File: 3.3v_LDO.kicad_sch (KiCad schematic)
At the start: 7 parts, among them U2 LP2985-3.3

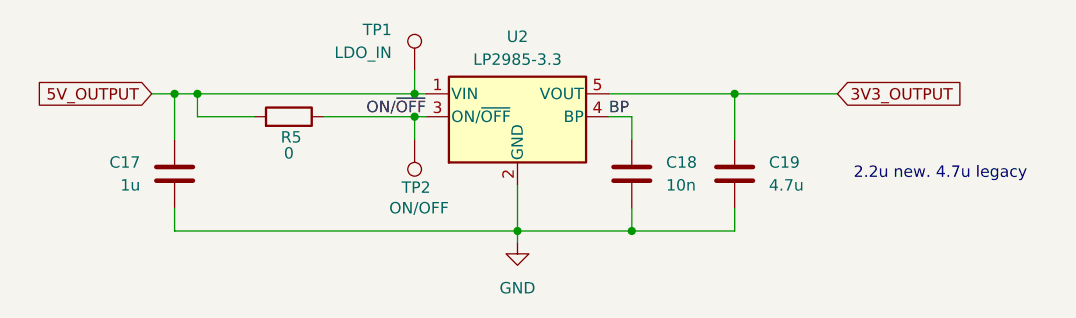
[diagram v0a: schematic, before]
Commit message: schematic for new DF11 and WJ127 connectors
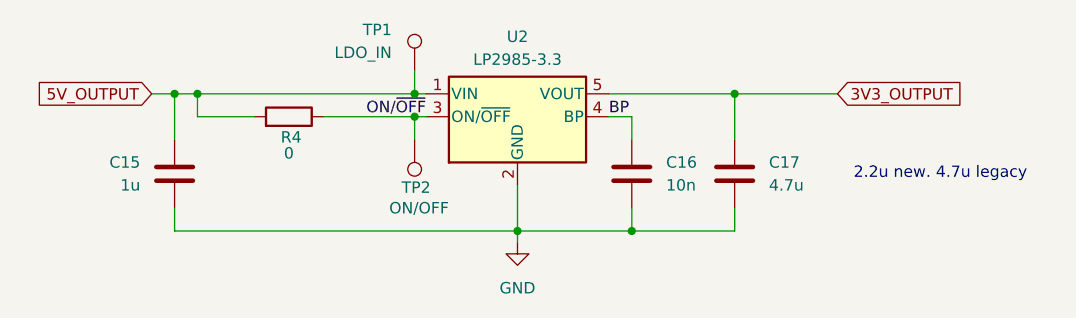
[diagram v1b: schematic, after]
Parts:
- renumbered C17 to C15, C18 to C16, C19 to C17, R5 to R4
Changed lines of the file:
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@@
 		(dnp no)
 		(fields_autoplaced yes)
-		(property "Reference" "#PWR011"
+		(property "Reference" "#PWR019"
 			(at 142.24 111.76 0)
 			(effects
@@
 			(project "ANTS-Power-board"
 				(path "/4d632659-7d2f-4407-ada5-b4e72f7be845/433705c3-0c9b-4b35-8329-f110f6531cb8"
-					(reference "#PWR011")
+					(reference "#PWR019")
 					(unit 1)
 				)
@@
 		(dnp no)
 		(fields_autoplaced yes)
-		(property "Reference" "C19"
+		(property "Reference" "C17"
 			(at 170.18 96.5199 0)
 			(effects
@@
 			(project "ANTS-Power-board"
 				(path "/4d632659-7d2f-4407-ada5-b4e72f7be845/433705c3-0c9b-4b35-8329-f110f6531cb8"
-					(reference "C19")
+					(reference "C17")
 					(unit 1)
 				)
@@
 		(dnp no)
 		(fields_autoplaced yes)
-		(property "Reference" "C18"
+		(property "Reference" "C16"
 			(at 158.75 96.5199 0)
 			(effects
@@
 			(project ""
 				(path "/4d632659-7d2f-4407-ada5-b4e72f7be845/433705c3-0c9b-4b35-8329-f110f6531cb8"
-					(reference "C18")
+					(reference "C16")
 					(unit 1)
 				)
@@
 		(on_board yes)
 		(dnp no)
-		(property "Reference" "R5"
+		(property "Reference" "R4"
 			(at 117.094 93.726 90)
 			(effects
@@
 			(project ""
 				(path "/4d632659-7d2f-4407-ada5-b4e72f7be845/433705c3-0c9b-4b35-8329-f110f6531cb8"
-					(reference "R5")
+					(reference "R4")
 					(unit 1)
 				)
@@
 		(on_board yes)
 		(dnp no)
-		(property "Reference" "C17"
+		(property "Reference" "C15"
 			(at 100.33 96.5199 0)
 			(effects
@@
 			(project ""
 				(path "/4d632659-7d2f-4407-ada5-b4e72f7be845/433705c3-0c9b-4b35-8329-f110f6531cb8"
-					(reference "C17")
-					(unit 1)
-				)
+					(reference "C15")
+					(unit 1)
+				)
